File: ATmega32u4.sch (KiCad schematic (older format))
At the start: 30 parts, among them J1 USB_B_Mini, J2 AVR-ISP-6, SW70 SW_Push, U4 ATmega32U4-MU, Y1 16MHz

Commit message: Redo the LED matrix
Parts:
- U4: symbol Global_MobiFlight_panel_parts:ATmega32U4-MU -> Collins-FMS-3000-rescue:ATmega32U4-MU-Global_MobiFlight_panel_parts
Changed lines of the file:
@@
 $Descr A4 11693 8268
 encoding utf-8
-Sheet 4 4
+Sheet 3 4
 Title ""
 Date ""
@@
 $EndDescr
 $Comp
-L Global_MobiFlight_panel_parts:ATmega32U4-MU U?
+L Collins-FMS-3000-rescue:ATmega32U4-MU-Global_MobiFlight_panel_parts U?
 U 1 1 61F97DC3
 P 1800 3000

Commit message: Much PCB layout
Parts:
- removed U4: ATmega32U4-MU, Package_DFN_QFN:QFN-44-1EP_7x7mm_P0.5mm_EP5.2x5.2mm, symbol Collins-FMS-3000-rescue:ATmega32U4-MU-Global_MobiFlight_panel_parts
- added U1: ATmega32U4-MU, Package_DFN_QFN:QFN-44-1EP_7x7mm_P0.5mm_EP5.2x5.2mm, symbol Collins-FMS-3000:ATmega32U4-MU
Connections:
- wire segments 82 -> 80
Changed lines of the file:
@@
 Comment4 ""
 $EndDescr
-$Comp
-L Collins-FMS-3000-rescue:ATmega32U4-MU-Global_MobiFlight_panel_parts U?
-U 1 1 61F97DC3
-P 1800 3000
-AR Path="/61F97DC3" Ref="U?"  Part="1"
-AR Path="/61F7F1B9/61F97DC3" Ref="U4"  Part="1"
-F 0 "U4" H 1900 1250 50  0000 L CNN
-F 1 "ATmega32U4-MU" H 1900 1150 50  0000 L CNN
-F 2 "Package_DFN_QFN:QFN-44-1EP_7x7mm_P0.5mm_EP5.2x5.2mm" H 1800 750 50  0001 C CIN
-F 3 "http://ww1.microchip.com/downloads/en/DeviceDoc/Atmel-7766-8-bit-AVR-ATmega16U4-32U4_Datasheet.pdf" H 1800 3000 50  0001 C CNN
-	1    1800 3000
-	1    0    0    -1
-$EndComp
 Text GLabel 950  1500 0    50   Input ~ 0
 RESET
-Wire Wire Line
-	1750 1200 1850 1200
-Connection ~ 1850 1200
-Wire Wire Line
-	1850 1200 1900 1200
-Connection ~ 1950 1200
-Wire Wire Line
-	1950 1200 2050 1200
 $Comp
 L power:+5V #PWR?
@@
 $EndComp
 Connection ~ 1900 1200
-Wire Wire Line
-	1900 1200 1950 1200
 $Comp
 L Device:C_Small C?
@@
 Text HLabel 2400 2700 2    50   Output ~ 0
 SCK
+Wire Wire Line
+	1900 1200 1950 1200
+$Comp
+L Collins-FMS-3000:ATmega32U4-MU U1
+U 1 1 618B76D9
+P 1800 3000
+F 0 "U1" H 1900 1250 50  0000 L CNN
+F 1 "ATmega32U4-MU" H 1900 1150 50  0000 L CNN
+F 2 "Package_DFN_QFN:QFN-44-1EP_7x7mm_P0.5mm_EP5.2x5.2mm" H 1800 750 50  0001 C CIN
+F 3 "http://ww1.microchip.com/downloads/en/DeviceDoc/Atmel-7766-8-bit-AVR-ATmega16U4-32U4_Datasheet.pdf" H 1800 3000 50  0001 C CNN
+	1    1800 3000
+	1    0    0    -1
+$EndComp
+Wire Wire Line
+	1850 1200 1900 1200
 $EndSCHEMATC

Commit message: Lots of PCB layout
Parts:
- U1: footprint Package_DFN_QFN:QFN-44-1EP_7x7mm_P0.5mm_EP5.2x5.2mm -> Package_QFP:TQFP-44-1EP_10x10mm_P0.8mm_EP4.5x4.5mm
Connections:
- net +5V: now also U1.14 (VCC), U1.44 (AVCC)
- net SCK: no longer U1.18 (PD0#)
- new net SCL: U1.18 (PD0#)
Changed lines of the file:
@@
 	1    0    0    -1
 $EndComp
-Text HLabel 2400 2800 2    50   BiDi ~ 0
-SDA
-Text HLabel 2400 2700 2    50   Output ~ 0
-SCK
 Wire Wire Line
 	1900 1200 1950 1200
@@
 F 0 "U1" H 1900 1250 50  0000 L CNN
 F 1 "ATmega32U4-MU" H 1900 1150 50  0000 L CNN
-F 2 "Package_DFN_QFN:QFN-44-1EP_7x7mm_P0.5mm_EP5.2x5.2mm" H 1800 750 50  0001 C CIN
+F 2 "Package_QFP:TQFP-44-1EP_10x10mm_P0.8mm_EP4.5x4.5mm" H 1800 750 50  0001 C CIN
 F 3 "http://ww1.microchip.com/downloads/en/DeviceDoc/Atmel-7766-8-bit-AVR-ATmega16U4-32U4_Datasheet.pdf" H 1800 3000 50  0001 C CNN
 	1    1800 3000
@@
 Wire Wire Line
 	1850 1200 1900 1200
+Wire Wire Line
+	1750 1200 1850 1200
+Connection ~ 1850 1200
+Wire Wire Line
+	2050 1200 1950 1200
+Connection ~ 1950 1200
+Text HLabel 2600 2700 2    50   Output ~ 0
+SCL
+Text HLabel 2600 2800 2    50   BiDi ~ 0
+SDA
+Wire Wire Line
+	2400 2700 2600 2700
+Wire Wire Line
+	2400 2800 2600 2800
+Text Label 2550 2700 2    50   ~ 0
+SCL
+Text Label 2550 2800 2    50   ~ 0
+SDA
 $EndSCHEMATC

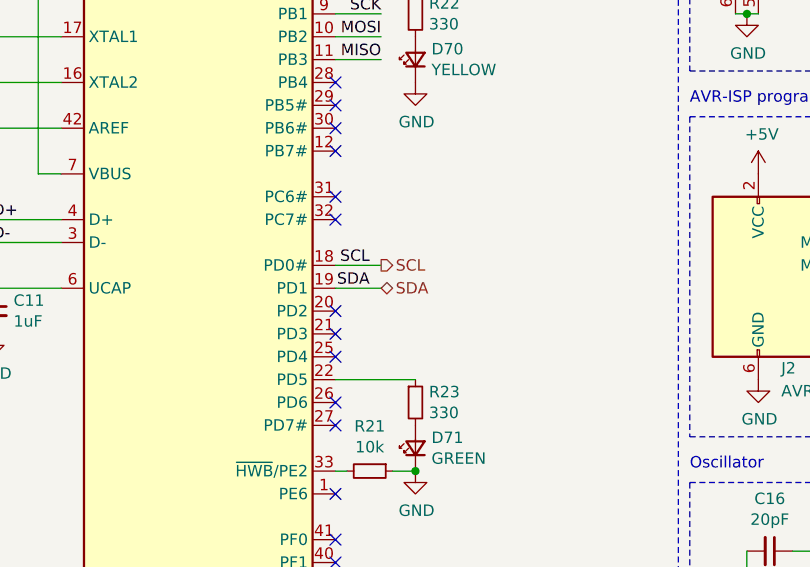
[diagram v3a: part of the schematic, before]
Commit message: New LED chip, tons of routing on the board
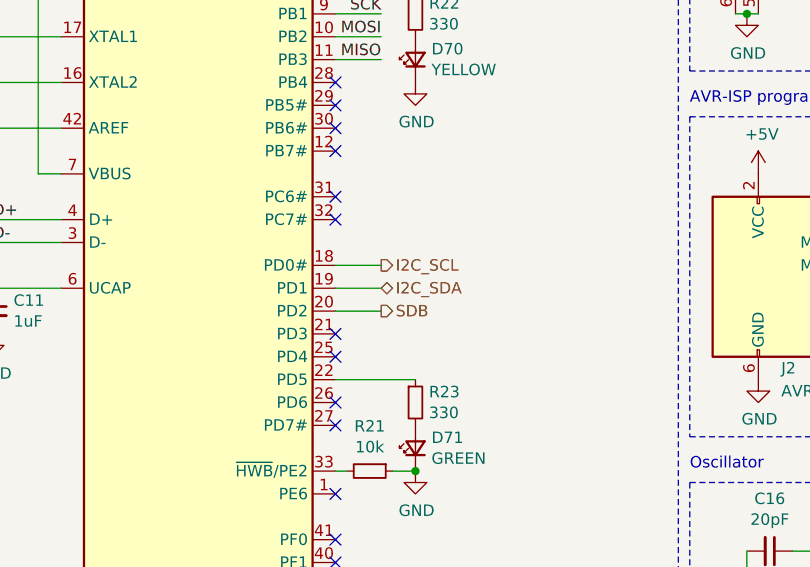
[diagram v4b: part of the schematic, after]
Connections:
- net SDB: now reaches U1.20 (PD2)
- net SCL renamed I2C_SCL
- net SDA renamed I2C_SDA
- no-connect marks 19 -> 18
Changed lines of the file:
@@
 NoConn ~ 2400 2400
 NoConn ~ 2400 2500
-NoConn ~ 2400 2900
 NoConn ~ 2400 3000
 NoConn ~ 2400 3100
@@
 Connection ~ 1950 1200
 Text HLabel 2600 2700 2    50   Output ~ 0
-SCL
+I2C_SCL
 Text HLabel 2600 2800 2    50   BiDi ~ 0
-SDA
+I2C_SDA
 Wire Wire Line
 	2400 2700 2600 2700
 Wire Wire Line
 	2400 2800 2600 2800
-Text Label 2550 2700 2    50   ~ 0
-SCL
-Text Label 2550 2800 2    50   ~ 0
-SDA
+Wire Wire Line
+	2400 2900 2600 2900
+Text HLabel 2600 2900 2    50   Output ~ 0
+SDB
 $EndSCHEMATC

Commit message: More routing
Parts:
- added J3: Conn_01x04, Connector_PinHeader_2.54mm:PinHeader_1x04_P2.54mm_Vertical, symbol Connector_Generic:Conn_01x04
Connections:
- net GND: now also J3.4 (Pin_4)
- net I2C_SCL: now also J3.1 (Pin_1)
- net I2C_SDA: now also J3.2 (Pin_2)
- net SDB: now also J3.3 (Pin_3)
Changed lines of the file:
@@
 I2C_SDA
 Wire Wire Line
-	2400 2700 2600 2700
+	2400 2800 2500 2800
 Wire Wire Line
-	2400 2800 2600 2800
-Wire Wire Line
-	2400 2900 2600 2900
+	2400 2900 2550 2900
 Text HLabel 2600 2900 2    50   Output ~ 0
 SDB
+Wire Wire Line
+	2500 2800 2500 2750
+Wire Wire Line
+	2500 2750 3250 2750
+Wire Wire Line
+	3250 2750 3250 2800
+Connection ~ 2500 2800
+Wire Wire Line
+	2500 2800 2600 2800
+Wire Wire Line
+	2400 2700 2450 2700
+Wire Wire Line
+	2450 2700 2450 2650
+Wire Wire Line
+	2450 2650 3250 2650
+Wire Wire Line
+	3250 2650 3250 2700
+Connection ~ 2450 2700
+Wire Wire Line
+	2450 2700 2600 2700
+Wire Wire Line
+	2550 2900 2550 2850
+Wire Wire Line
+	2550 2850 3250 2850
+Wire Wire Line
+	3250 2850 3250 2900
+Connection ~ 2550 2900
+Wire Wire Line
+	2550 2900 2600 2900
+$Comp
+L Connector_Generic:Conn_01x04 J3
+U 1 1 618E5A1D
+P 3450 2800
+F 0 "J3" H 3400 2500 50  0000 L CNN
+F 1 "Conn_01x04" H 3400 2400 50  0000 L CNN
+F 2 "Connector_PinHeader_2.54mm:PinHeader_1x04_P2.54mm_Vertical" H 3450 2800 50  0001 C CNN
+F 3 "~" H 3450 2800 50  0001 C CNN
+	1    3450 2800
+	1    0    0    -1
+$EndComp
+$Comp
+L power:GND #PWR0105
+U 1 1 618E6506
+P 3250 3000
+F 0 "#PWR0105" H 3250 2750 50  0001 C CNN
+F 1 "GND" H 3255 2827 50  0000 C CNN
+F 2 "" H 3250 3000 50  0001 C CNN
+F 3 "" H 3250 3000 50  0001 C CNN
+	1    3250 3000
+	1    0    0    -1
+$EndComp
 $EndSCHEMATC

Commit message: Fully routed
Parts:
- added R1, R2: 2k, Resistor_SMD:R_0805_2012Metric_Pad1.20x1.40mm_HandSolder, symbol Device:R_Small
- added R3: 100k, Resistor_SMD:R_0402_1005Metric, symbol Device:R_Small
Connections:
- net +5V: now also R1.1, R2.1
- net GND: now also R3.2
- net I2C_SCL: now also R1.2
- net I2C_SDA: now also R2.2
- net SDB: now also R3.1
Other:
- moved on the sheet: J3
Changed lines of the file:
@@
 Wire Wire Line
 	2400 2800 2500 2800
-Wire Wire Line
-	2400 2900 2550 2900
-Text HLabel 2600 2900 2    50   Output ~ 0
+Text HLabel 3150 2900 2    50   Output ~ 0
 SDB
 Wire Wire Line
 	2500 2800 2500 2750
 Wire Wire Line
-	2500 2750 3250 2750
-Wire Wire Line
-	3250 2750 3250 2800
+	2500 2750 3000 2750
 Connection ~ 2500 2800
 Wire Wire Line
@@
 Wire Wire Line
 	2450 2700 2450 2650
-Wire Wire Line
-	2450 2650 3250 2650
-Wire Wire Line
-	3250 2650 3250 2700
 Connection ~ 2450 2700
 Wire Wire Line
 	2450 2700 2600 2700
-Wire Wire Line
-	2550 2900 2550 2850
-Wire Wire Line
-	2550 2850 3250 2850
-Wire Wire Line
-	3250 2850 3250 2900
-Connection ~ 2550 2900
-Wire Wire Line
-	2550 2900 2600 2900
 $Comp
 L Connector_Generic:Conn_01x04 J3
 U 1 1 618E5A1D
-P 3450 2800
-F 0 "J3" H 3400 2500 50  0000 L CNN
-F 1 "Conn_01x04" H 3400 2400 50  0000 L CNN
-F 2 "Connector_PinHeader_2.54mm:PinHeader_1x04_P2.54mm_Vertical" H 3450 2800 50  0001 C CNN
-F 3 "~" H 3450 2800 50  0001 C CNN
-	1    3450 2800
+P 3600 2800
+F 0 "J3" H 3550 2500 50  0000 L CNN
+F 1 "Conn_01x04" H 3400 3050 50  0000 L CNN
+F 2 "Connector_PinHeader_2.54mm:PinHeader_1x04_P2.54mm_Vertical" H 3600 2800 50  0001 C CNN
+F 3 "~" H 3600 2800 50  0001 C CNN
+	1    3600 2800
 	1    0    0    -1
 $EndComp
@@
 L power:GND #PWR0105
 U 1 1 618E6506
-P 3250 3000
-F 0 "#PWR0105" H 3250 2750 50  0001 C CNN
-F 1 "GND" H 3255 2827 50  0000 C CNN
-F 2 "" H 3250 3000 50  0001 C CNN
-F 3 "" H 3250 3000 50  0001 C CNN
-	1    3250 3000
+P 3400 3000
+F 0 "#PWR0105" H 3400 2750 50  0001 C CNN
+F 1 "GND" H 3405 2827 50  0000 C CNN
+F 2 "" H 3400 3000 50  0001 C CNN
+F 3 "" H 3400 3000 50  0001 C CNN
+	1    3400 3000
 	1    0    0    -1
 $EndComp
+$Comp
+L Device:R_Small R1
+U 1 1 6192799E
+P 2700 2500
+F 0 "R1" H 2759 2546 50  0000 L CNN
+F 1 "2k" H 2759 2455 50  0000 L CNN
+F 2 "Resistor_SMD:R_0805_2012Metric_Pad1.20x1.40mm_HandSolder" H 2700 2500 50  0001 C CNN
+F 3 "~" H 2700 2500 50  0001 C CNN
+	1    2700 2500
+	1    0    0    -1
+$EndComp
+$Comp
+L Device:R_Small R2
+U 1 1 619283FA
+P 3000 2500
+F 0 "R2" H 3059 2546 50  0000 L CNN
+F 1 "2k" H 3059 2455 50  0000 L CNN
+F 2 "Resistor_SMD:R_0805_2012Metric_Pad1.20x1.40mm_HandSolder" H 3000 2500 50  0001 C CNN
+F 3 "~" H 3000 2500 50  0001 C CNN
+	1    3000 2500
+	1    0    0    -1
+$EndComp
+Wire Wire Line
+	2450 2650 2700 2650
+Wire Wire Line
+	2700 2650 2700 2600
+Connection ~ 2700 2650
+$Comp
+L power:+5V #PWR06
+U 1 1 6193D3D5
+P 2850 2400
+F 0 "#PWR06" H 2850 2250 50  0001 C CNN
+F 1 "+5V" H 2865 2573 50  0000 C CNN
+F 2 "" H 2850 2400 50  0001 C CNN
+F 3 "" H 2850 2400 50  0001 C CNN
+	1    2850 2400
+	1    0    0    -1
+$EndComp
+Wire Wire Line
+	3000 2750 3000 2600
+Connection ~ 3000 2750
+Wire Wire Line
+	2700 2400 2850 2400
+Connection ~ 2850 2400
+Wire Wire Line
+	2850 2400 3000 2400
+$Comp
+L power:GND #PWR?
+U 1 1 6195136F
+P 3100 3150
+AR Path="/6195136F" Ref="#PWR?"  Part="1"
+AR Path="/61F7F1B9/6195136F" Ref="#PWR012"  Part="1"
+F 0 "#PWR012" H 3100 2900 50  0001 C CNN
+F 1 "GND" H 3105 2977 50  0000 C CNN
+F 2 "" H 3100 3150 50  0001 C CNN
+F 3 "" H 3100 3150 50  0001 C CNN
+	1    3100 3150
+	1    0    0    -1
+$EndComp
+Wire Wire Line
+	3400 2850 3400 2900
+Wire Wire Line
+	2400 2900 3100 2900
+Connection ~ 3100 2900
+Wire Wire Line
+	3100 2900 3150 2900
+Wire Wire Line
+	3400 2850 3100 2850
+Wire Wire Line
+	3100 2850 3100 2900
+Wire Wire Line
+	3400 2750 3400 2800
+Wire Wire Line
+	3000 2750 3400 2750
+Wire Wire Line
+	3400 2650 3400 2700
+Wire Wire Line
+	2700 2650 3400 2650
+$Comp
+L Device:R_Small R?
+U 1 1 61951368
+P 3100 3050
+AR Path="/61951368" Ref="R?"  Part="1"
+AR Path="/61F7F1B9/61951368" Ref="R3"  Part="1"
+F 0 "R3" H 3159 3096 50  0000 L CNN
+F 1 "100k" H 3159 3005 50  0000 L CNN
+F 2 "Resistor_SMD:R_0402_1005Metric" H 3100 3050 50  0001 C CNN
+F 3 "~" H 3100 3050 50  0001 C CNN
+	1    3100 3050
+	1    0    0    -1
+$EndComp
+Wire Wire Line
+	3100 2950 3100 2900
 $EndSCHEMATC

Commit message: Assign JLCPCB part numbers
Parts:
- C10, C18: JLC (none) -> 0402; LCSC (none) -> C15525
- C11, C9: JLC (none) -> 0402; LCSC (none) -> C52923
- C12, C13, C14, C15, C19, C20: JLC (none) -> 0402; LCSC (none) -> C1525
- C16, C17: JLC (none) -> 0402; LCSC (none) -> C1554
- D70: JLC (none) -> 0603; LCSC (none) -> C72038
- D71, D73: JLC (none) -> 0603
- D72: JLC (none) -> SOD-323F; LCSC (none) -> C2128
- FB1: JLC (none) -> 0805; LCSC (none) -> C72043
- R1, R2: JLC (none) -> 0805; LCSC (none) -> C17604
- R21, R27: JLC (none) -> 0402; LCSC (none) -> C25744
- R22, R23, R26: JLC (none) -> 0402; LCSC (none) -> C25104
- R24, R25: JLC (none) -> 0402; LCSC (none) -> 0402
- R28: JLC (none) -> 0402; LCSC (none) -> C11702
- R3: JLC (none) -> 0402; LCSC (none) -> C25741
- Y1: JLC (none) -> SMD-CRY-3225_4P; LCSC (none) -> C13738
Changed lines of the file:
@@
 F 2 "Capacitor_SMD:C_0402_1005Metric" H 800 1000 50  0001 C CNN
 F 3 "~" H 800 1000 50  0001 C CNN
+F 4 "0402" H 800 1000 50  0001 C CNN "JLC"
+F 5 "C15525" H 800 1000 50  0001 C CNN "LCSC"
 	1    800  1000
 	1    0    0    -1
@@
 F 2 "Capacitor_SMD:C_0402_1005Metric" H 700 2200 50  0001 C CNN
 F 3 "~" H 700 2200 50  0001 C CNN
+F 4 "0402" H 700 2200 50  0001 C CNN "JLC"
+F 5 "C52923" H 700 2200 50  0001 C CNN "LCSC"
 	1    700  2200
 	1    0    0    -1
@@
 F 2 "Capacitor_SMD:C_0402_1005Metric" H 900 2900 50  0001 C CNN
 F 3 "~" H 900 2900 50  0001 C CNN
+F 4 "0402" H 900 2900 50  0001 C CNN "JLC"
+F 5 "C52923" H 900 2900 50  0001 C CNN "LCSC"
 	1    900  2900
 	1    0    0    -1
@@
 F 2 "Resistor_SMD:R_0402_1005Metric" H 2750 1600 50  0001 C CNN
 F 3 "~" H 2750 1600 50  0001 C CNN
+F 4 "0402" H 2750 1600 50  0001 C CNN "JLC"
+F 5 "C25104" H 2750 1600 50  0001 C CNN "LCSC"
 	1    2750 1600
 	1    0    0    -1
@@
 F 2 "Collins-FMS-3000:LED_0603_1608Metric" V 2750 1800 50  0001 C CNN
 F 3 "~" V 2750 1800 50  0001 C CNN
+F 4 "0603" H 2750 1800 50  0001 C CNN "JLC"
+F 5 "C72038" H 2750 1800 50  0001 C CNN "LCSC"
 	1    2750 1800
 	0    -1   -1   0
@@
 F 2 "Resistor_SMD:R_0402_1005Metric" H 2750 3300 50  0001 C CNN
 F 3 "~" H 2750 3300 50  0001 C CNN
+F 4 "0402" H 2750 3300 50  0001 C CNN "JLC"
+F 5 "C25104" H 2750 3300 50  0001 C CNN "LCSC"
 	1    2750 3300
 	1    0    0    -1
@@
 F 2 "Collins-FMS-3000:LED_0603_1608Metric" V 2750 3500 50  0001 C CNN
 F 3 "~" V 2750 3500 50  0001 C CNN
+F 4 "0603" H 2750 3500 50  0001 C CNN "JLC"
 	1    2750 3500
 	0    -1   -1   0
@@
 F 2 "Resistor_SMD:R_0402_1005Metric" H 2550 3600 50  0001 C CNN
 F 3 "~" H 2550 3600 50  0001 C CNN
+F 4 "0402" H 2550 3600 50  0001 C CNN "JLC"
+F 5 "C25744" H 2550 3600 50  0001 C CNN "LCSC"
 	1    2550 3600
 	0    1    1    0
@@
 F 2 "Capacitor_SMD:C_0402_1005Metric" H 2300 1000 50  0001 C CNN
 F 3 "~" H 2300 1000 50  0001 C CNN
+F 4 "0402" H 2300 1000 50  0001 C CNN "JLC"
+F 5 "C1525" H 2300 1000 50  0001 C CNN "LCSC"
 	1    2300 1000
 	1    0    0    -1
@@
 F 2 "Capacitor_SMD:C_0402_1005Metric" H 2700 1000 50  0001 C CNN
 F 3 "~" H 2700 1000 50  0001 C CNN
+F 4 "0402" H 2700 1000 50  0001 C CNN "JLC"
+F 5 "C1525" H 2700 1000 50  0001 C CNN "LCSC"
 	1    2700 1000
 	1    0    0    -1
@@
 F 2 "Capacitor_SMD:C_0402_1005Metric" H 3100 1000 50  0001 C CNN
 F 3 "~" H 3100 1000 50  0001 C CNN
+F 4 "0402" H 3100 1000 50  0001 C CNN "JLC"
+F 5 "C1525" H 3100 1000 50  0001 C CNN "LCSC"
 	1    3100 1000
 	1    0    0    -1
@@
 F 2 "Capacitor_SMD:C_0402_1005Metric" H 3500 1000 50  0001 C CNN
 F 3 "~" H 3500 1000 50  0001 C CNN
+F 4 "0402" H 3500 1000 50  0001 C CNN "JLC"
+F 5 "C1525" H 3500 1000 50  0001 C CNN "LCSC"
 	1    3500 1000
 	1    0    0    -1
@@
 F 2 "Capacitor_SMD:C_0805_2012Metric" V 4880 1000 50  0001 C CNN
 F 3 "~" H 4950 1000 50  0001 C CNN
+F 4 "0805" H 4950 1000 50  0001 C CNN "JLC"
+F 5 "C72043" H 4950 1000 50  0001 C CNN "LCSC"
 	1    4950 1000
 	0    1    1    0
@@
 F 2 "Resistor_SMD:R_0402_1005Metric" H 4950 1350 50  0001 C CNN
 F 3 "~" H 4950 1350 50  0001 C CNN
+F 4 "0402" H 4950 1350 50  0001 C CNN "JLC"
+F 5 "0402" H 4950 1350 50  0001 C CNN "LCSC"
 	1    4950 1350
 	0    1    1    0
@@
 F 2 "Resistor_SMD:R_0402_1005Metric" H 4950 1650 50  0001 C CNN
 F 3 "~" H 4950 1650 50  0001 C CNN
+F 4 "0402" H 4950 1650 50  0001 C CNN "JLC"
+F 5 "0402" H 4950 1650 50  0001 C CNN "LCSC"
 	1    4950 1650
 	0    1    1    0
@@
 F 2 "Capacitor_SMD:C_0402_1005Metric" H 5450 1100 50  0001 C CNN
 F 3 "~" H 5450 1100 50  0001 C CNN
+F 4 "0402" H 5450 1100 50  0001 C CNN "JLC"
+F 5 "C15525" H 5450 1100 50  0001 C CNN "LCSC"
 	1    5450 1100
 	1    0    0    -1
@@
 F 2 "Resistor_SMD:R_0402_1005Metric" H 5900 1100 50  0001 C CNN
 F 3 "~" H 5900 1100 50  0001 C CNN
+F 4 "0402" H 5900 1100 50  0001 C CNN "JLC"
+F 5 "C11702" H 5900 1100 50  0001 C CNN "LCSC"
 	1    5900 1100
 	1    0    0    -1
@@
 F 2 "Collins-FMS-3000:LED_0603_1608Metric" V 5900 1300 50  0001 C CNN
 F 3 "~" V 5900 1300 50  0001 C CNN
+F 4 "0603" H 5900 1300 50  0001 C CNN "JLC"
 	1    5900 1300
 	0    -1   -1   0
@@
 F 2 "Crystal:Crystal_SMD_3225-4Pin_3.2x2.5mm" H 4750 4200 50  0001 C CNN
 F 3 "~" H 4750 4200 50  0001 C CNN
+F 4 "SMD-CRY-3225_4P" H 4750 4200 50  0001 C CNN "JLC"
+F 5 "C13738" H 4750 4200 50  0001 C CNN "LCSC"
 	1    4750 4200
 	0    1    1    0
@@
 F 2 "Capacitor_SMD:C_0402_1005Metric" H 4300 3950 50  0001 C CNN
 F 3 "~" H 4300 3950 50  0001 C CNN
+F 4 "0402" H 4300 3950 50  0001 C CNN "JLC"
+F 5 "C1554" H 4300 3950 50  0001 C CNN "LCSC"
 	1    4300 3950
 	0    1    1    0
@@
 F 2 "Capacitor_SMD:C_0402_1005Metric" H 4300 4450 50  0001 C CNN
 F 3 "~" H 4300 4450 50  0001 C CNN
+F 4 "0402" H 4300 4450 50  0001 C CNN "JLC"
+F 5 "C1554" H 4300 4450 50  0001 C CNN "LCSC"
 	1    4300 4450
 	0    1    1    0
@@
 F 2 "Capacitor_SMD:C_0402_1005Metric" H 6200 2400 50  0001 C CNN
 F 3 "~" H 6200 2400 50  0001 C CNN
+F 4 "0402" H 6200 2400 50  0001 C CNN "JLC"
+F 5 "C1525" H 6200 2400 50  0001 C CNN "LCSC"
 	1    6200 2400
 	1    0    0    -1
@@
 F 2 "Capacitor_SMD:C_0402_1005Metric" H 5800 2400 50  0001 C CNN
 F 3 "~" H 5800 2400 50  0001 C CNN
+F 4 "0402" H 5800 2400 50  0001 C CNN "JLC"
+F 5 "C1525" H 5800 2400 50  0001 C CNN "LCSC"
 	1    5800 2400
 	1    0    0    -1
@@
 F 2 "Resistor_SMD:R_0402_1005Metric" H 5400 2400 50  0001 C CNN
 F 3 "~" H 5400 2400 50  0001 C CNN
+F 4 "0402" H 5400 2400 50  0001 C CNN "JLC"
+F 5 "C25744" H 5400 2400 50  0001 C CNN "LCSC"
 	1    5400 2400
 	1    0    0    -1
@@
 F 2 "Resistor_SMD:R_0402_1005Metric" H 5250 3200 50  0001 C CNN
 F 3 "~" H 5250 3200 50  0001 C CNN
+F 4 "0402" H 5250 3200 50  0001 C CNN "JLC"
+F 5 "C25104" H 5250 3200 50  0001 C CNN "LCSC"
 	1    5250 3200
 	0    -1   -1   0
@@
 F 2 "Diode_SMD:D_SOD-323F" V 5150 2400 50  0001 C CNN
 F 3 "~" V 5150 2400 50  0001 C CNN
+F 4 "SOD-323F" H 5150 2400 50  0001 C CNN "JLC"
+F 5 "C2128" H 5150 2400 50  0001 C CNN "LCSC"
 	1    5150 2400
 	0    1    1    0
@@
 F 2 "Resistor_SMD:R_0805_2012Metric_Pad1.20x1.40mm_HandSolder" H 2700 2500 50  0001 C CNN
 F 3 "~" H 2700 2500 50  0001 C CNN
+F 4 "0805" H 2700 2500 50  0001 C CNN "JLC"
+F 5 "C17604" H 2700 2500 50  0001 C CNN "LCSC"
 	1    2700 2500
 	1    0    0    -1
@@
 F 2 "Resistor_SMD:R_0805_2012Metric_Pad1.20x1.40mm_HandSolder" H 3000 2500 50  0001 C CNN
 F 3 "~" H 3000 2500 50  0001 C CNN
+F 4 "0805" H 3000 2500 50  0001 C CNN "JLC"
+F 5 "C17604" H 3000 2500 50  0001 C CNN "LCSC"
 	1    3000 2500
 	1    0    0    -1
@@
 F 2 "Resistor_SMD:R_0402_1005Metric" H 3100 3050 50  0001 C CNN
 F 3 "~" H 3100 3050 50  0001 C CNN
+F 4 "0402" H 3100 3050 50  0001 C CNN "JLC"
+F 5 "C25741" H 3100 3050 50  0001 C CNN "LCSC"
 	1    3100 3050
 	1    0    0    -1

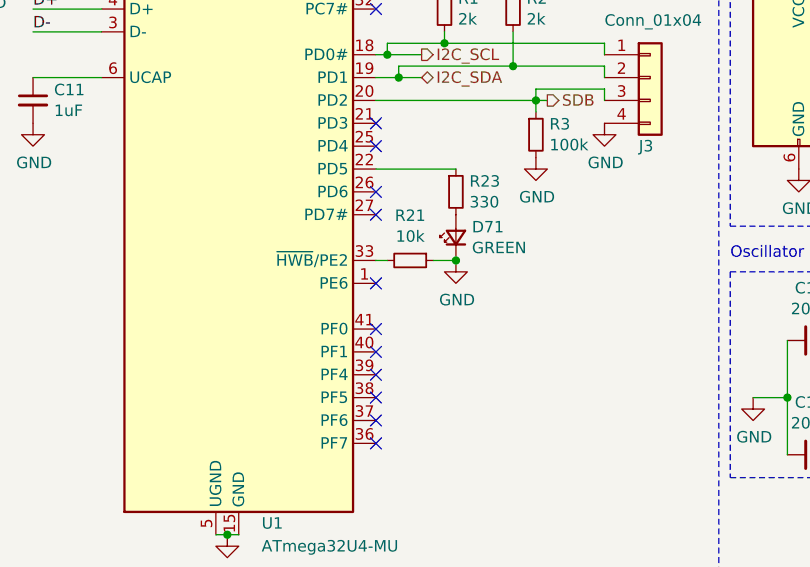
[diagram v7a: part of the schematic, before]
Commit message: Add INTB connection
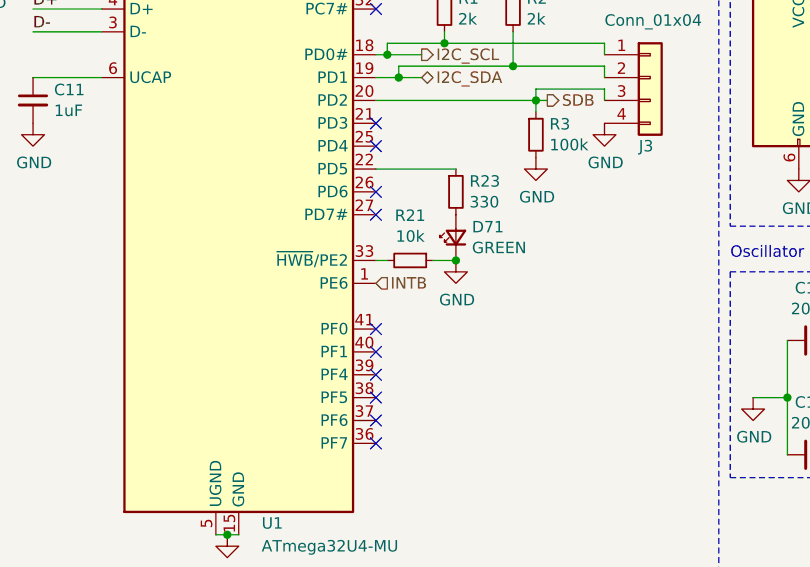
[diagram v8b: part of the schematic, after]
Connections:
- net INTB: now reaches U1.1 (PE6)
- no-connect marks 18 -> 17
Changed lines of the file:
@@
 NoConn ~ 2400 2400
 NoConn ~ 2400 2500
-NoConn ~ 2400 3000
 NoConn ~ 2400 3100
 NoConn ~ 2400 3300
 NoConn ~ 2400 3400
-NoConn ~ 2400 3700
 NoConn ~ 2400 3900
 NoConn ~ 2400 4000
@@
 Wire Wire Line
 	3100 2950 3100 2900
+Text HLabel 2400 3700 2    50   Input ~ 0
+INTB
+NoConn ~ 2400 3000
 $EndSCHEMATC
